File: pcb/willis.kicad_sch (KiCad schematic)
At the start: 111 parts, among them J1 SWD, J2 Battery, J3 USB-C Conn, J4 Battery JST, K1 KEYSW, K10 KEYSW, K11 KEYSW, K12 KEYSW, K13 KEYSW, K14 KEYSW, K15 KEYSW, K16 KEYSW, K17 KEYSW, K18 KEYSW, K19 KEYSW, K2 KEYSW, K20 KEYSW, K21 KEYSW, K22 KEYSW, K23 KEYSW, K24 KEYSW, K25 KEYSW, K26 KEYSW, K27 KEYSW, K28 KEYSW, K29 KEYSW, K3 KEYSW, K30 KEYSW, K31 KEYSW, K32 KEYSW, K33 KEYSW, K34 KEYSW, K35 KEYSW, K36 KEYSW, K37 KEYSW, K38 KEYSW, K4 KEYSW, K5 KEYSW, K6 KEYSW, K7 KEYSW, K8 KEYSW, K9 KEYSW, Q1 AO3407, SW1 SW_SPDT, U1 TP4054, U2 USBLC6-2SC6, U3 E73-2G4M08S1C-52840-TOP, X1 32.768kHz

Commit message: Add 3D model for E73, more routing fixes
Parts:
- removed JP1: Jumper_2_Bridged, Jumper:SolderJumper-2_P1.3mm_Bridged_Pad1.0x1.5mm, symbol Jumper:Jumper_2_Bridged
- removed SW1: SW_SPDT, Buttons_Switches:SW_SPDT+H-MSK12C01_hor(7pin_SMD), symbol Switch:SW_SPDT
- removed U3: E73-2G4M08S1C-52840-TOP, kbd:E73-2G4M08S1C-52840_TOP, symbol kbd_wl:E73-2G4M08S1C-52840-TOP
- added L3: 10uH, Inductor_SMD:L_0603_1608Metric_Pad1.05x0.95mm_HandSolder, symbol Device:L
- added RSW2: SW_PUSH, Button_Switch_SMD:SW_SPST_EVQP7C, symbol corne-cherry-rescue:SW_PUSH-kbd-corne-cherry-rescue
- added U3: E73-2G4M08S1C-52840, kbd:E73-2G4M08S1C-52840, symbol nrfmicro:E73-2G4M08S1C-52840
- H1, H2, H3, H4, J1, J2, K1, K10, K11, K12, K13, K14, K15, K16, K17, K18, K19, K2, K20, K21, K22, K23, K24, K25, K26, K27, K28, K29, K3, K30, K31, K32, K33, K34, K35, K36, K37, K38, K4, K5, K6, K7, K8, K9, S1, S2: now fitted
- RSW1: LCSC C388883 -> C388883; now fitted
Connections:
- net BLUE_LED: now also U3.2 (P1.10)
- net COL0: now also U3.1 (P1.11)
- net COL1: now also U3.3 (P0.03/AIN1)
- net COL2: now also U3.4 (P0.28/AIN4)
- net COL3: now also U3.6 (P1.13)
- net COL4: now also U3.7 (P0.02/AIN0)
- net COL5: now also U3.8 (P0.29/AIN5)
- net COL6: now also U3.33 (P0.13)
- net COL7: now also U3.35 (P0.24)
- net COL8: now also U3.41 (P0.09/NFC1)
- net COL9: now also U3.43 (P0.10/NFC2)
- net DATA+: now also U3.31 (USB_D+)
- net DATA-: now also U3.29 (USB_D-)
- net GND: now also L3.2, RSW2.1, U3.21 (GND), U3.24 (GND), U3.5 (GND)
- net ROW0: now also U3.9 (P0.31/AIN7)
- net ROW1: now also U3.10 (P0.30/AIN6)
- net ROW2: now also U3.15 (P0.05/AIN3)
- net ROW3: now also U3.17 (P1.09)
- net SWC: now also U3.39 (SWDCLK)
- net SWD: now also U3.37 (SWDIO)
- net VBUS: now also U3.27 (VBUS)
- net VDD: now also U3.19 (VDD)
- net VDDH: now also D40.1 (K), Q1.2 (S), U3.23 (VDDH)
- net XL1: now also U3.11 (P0.00/XL1)
- net XL2: now also U3.13 (P0.01/XL2)
- net at RSW1.2: now also U3.26 (P0.18/RESET)
- new net DCCH: L3.1, U3.25 (DCCH)
- new net SOFT_OFF: RSW2.2, U3.12 (P0.26)
- no-connect marks 4 -> 15
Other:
- moved on the sheet: C1, C4, X1

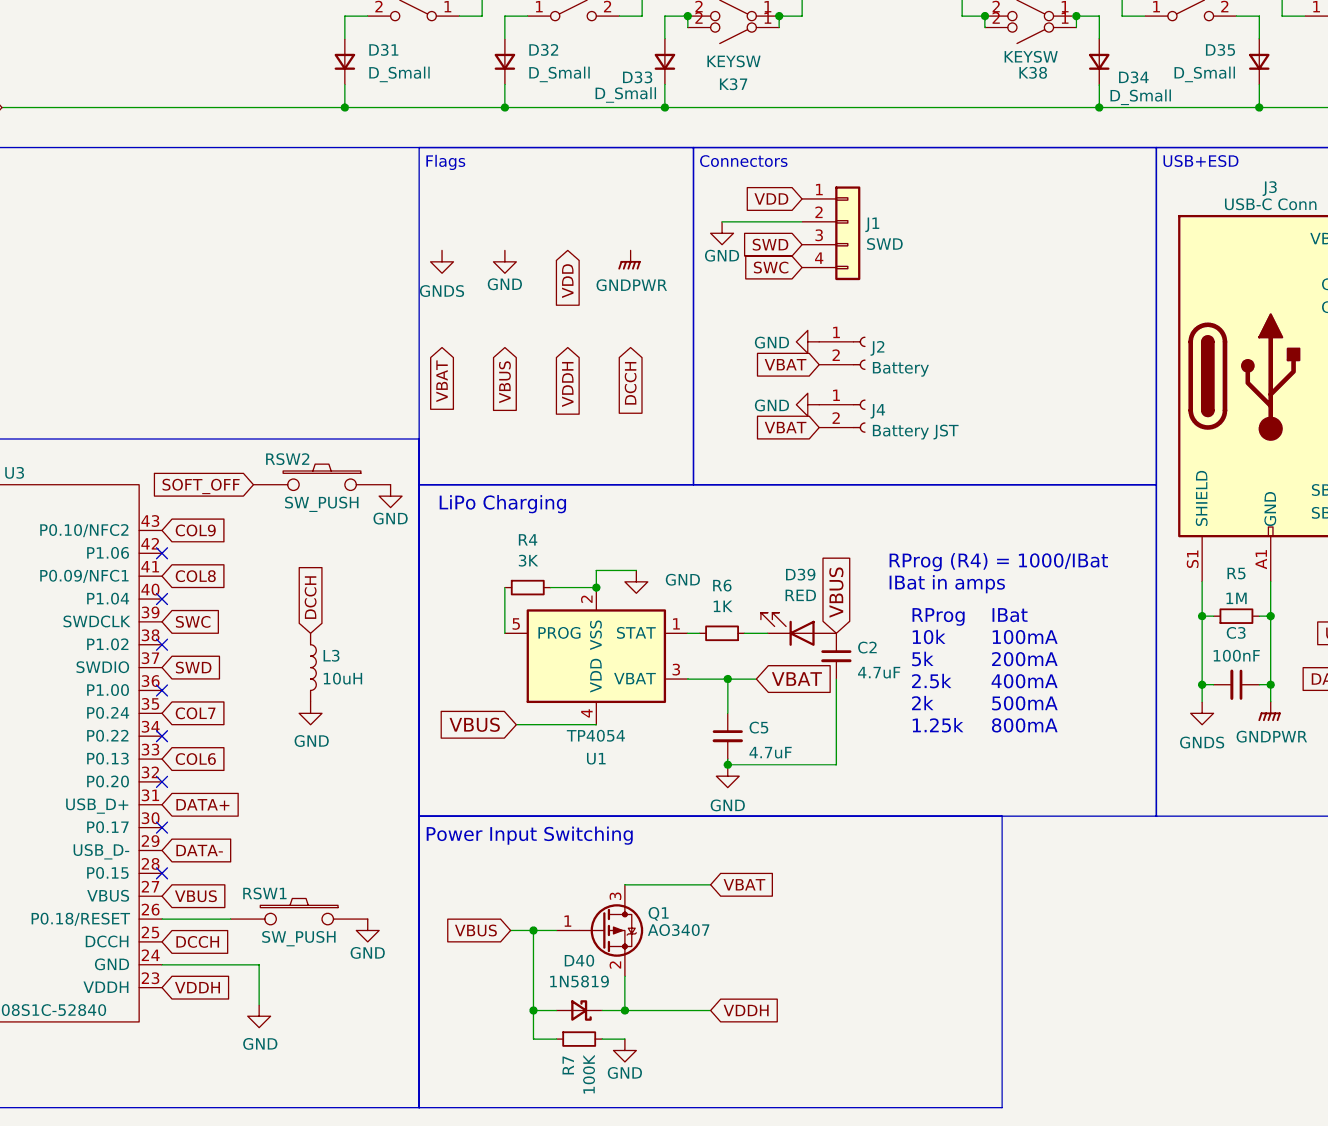
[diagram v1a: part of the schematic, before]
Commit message: Add TC2030 SWD footprint
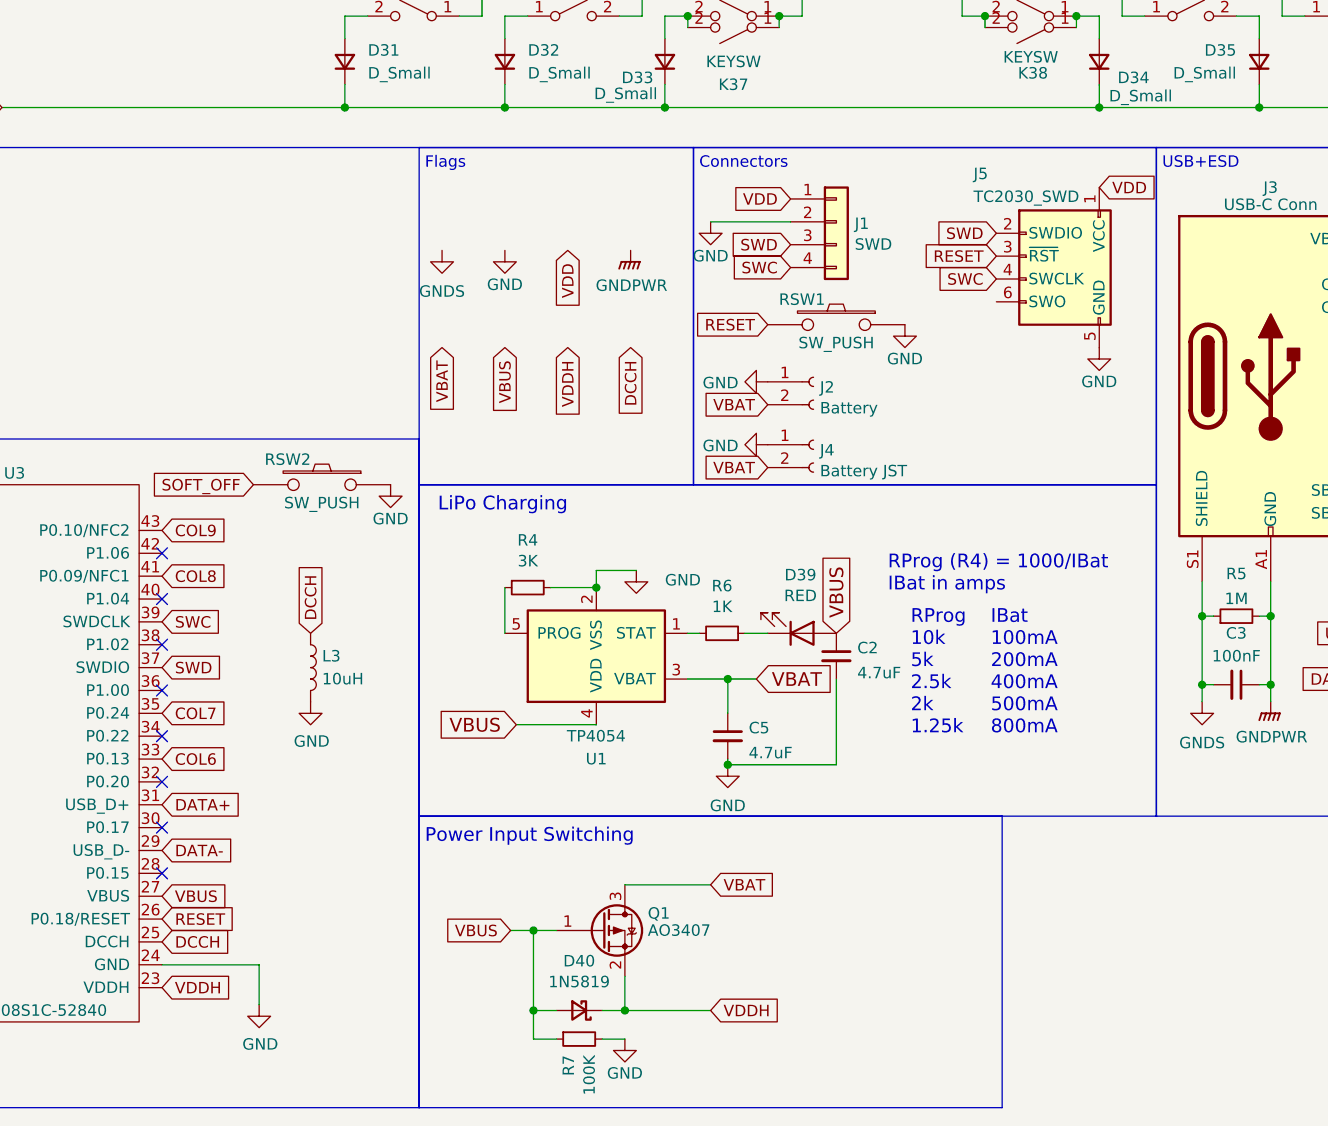
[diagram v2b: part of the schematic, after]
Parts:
- added J5: TC2030_SWD, PCM_marbastlib-various:CON_TC2030_outlined, symbol PCM_marbastlib-various:TC2030_SWD
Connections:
- net GND: now also J5.5 (GND)
- net SWC: now also J5.4 (SWCLK)
- net SWD: now also J5.2 (SWDIO)
- net VDD: now also J5.1 (VCC)
- net RESET: now reaches RSW1.2, U3.26 (P0.18/RESET)
- net RESET: now also J5.3 (~{RST})
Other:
- moved on the sheet: J1, J2, J4, RSW1

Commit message: V0.1: first manufactured revision
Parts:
- C1, C4: LCSC C1634 -> C1642
- U3: LCSC (none) -> C356849
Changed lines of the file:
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@@
 			)
 		)
-		(property "LCSC" "C1634"
+		(property "LCSC" "C1642"
 			(at 252.73 139.7 0)
 			(effects
@@
 			)
 		)
-		(property "LCSC" "C1634"
+		(property "LCSC" "C1642"
 			(at 252.73 152.4 0)
 			(effects
@@
 			(at 44.45 158.75 0)
 			(effects
+				(font
+					(size 1.27 1.27)
+				)
+				(hide yes)
+			)
+		)
+		(property "LCSC" "C356849"
+			(at 44.45 158.75 0)
+			(effects
